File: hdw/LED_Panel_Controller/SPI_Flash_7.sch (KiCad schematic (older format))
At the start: 14 parts

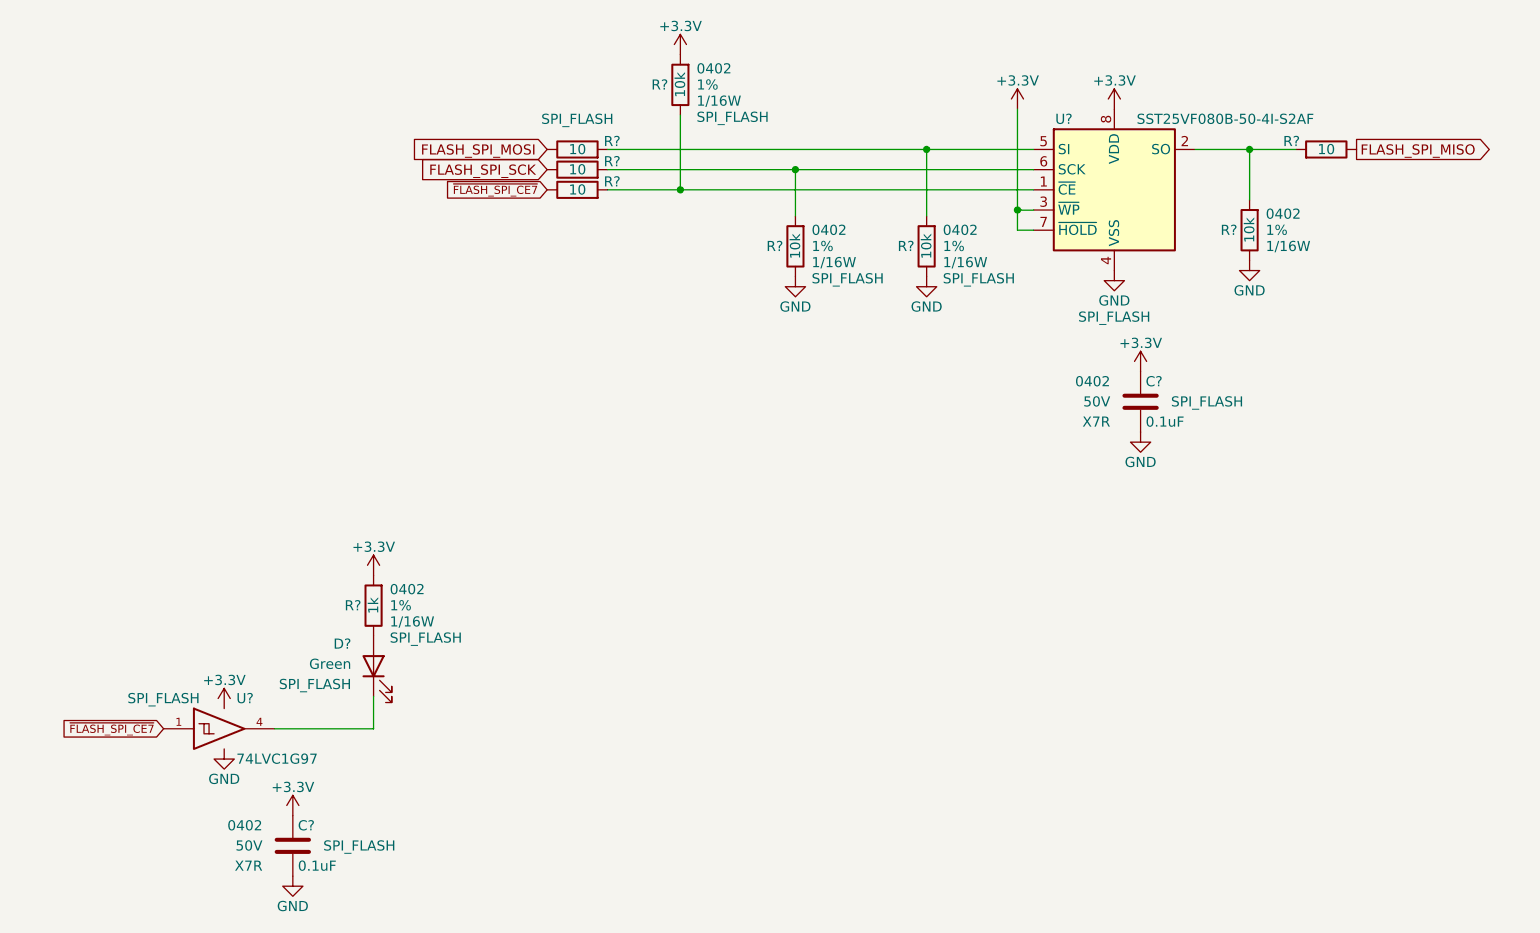
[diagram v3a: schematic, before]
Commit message: assigned I2C addresses
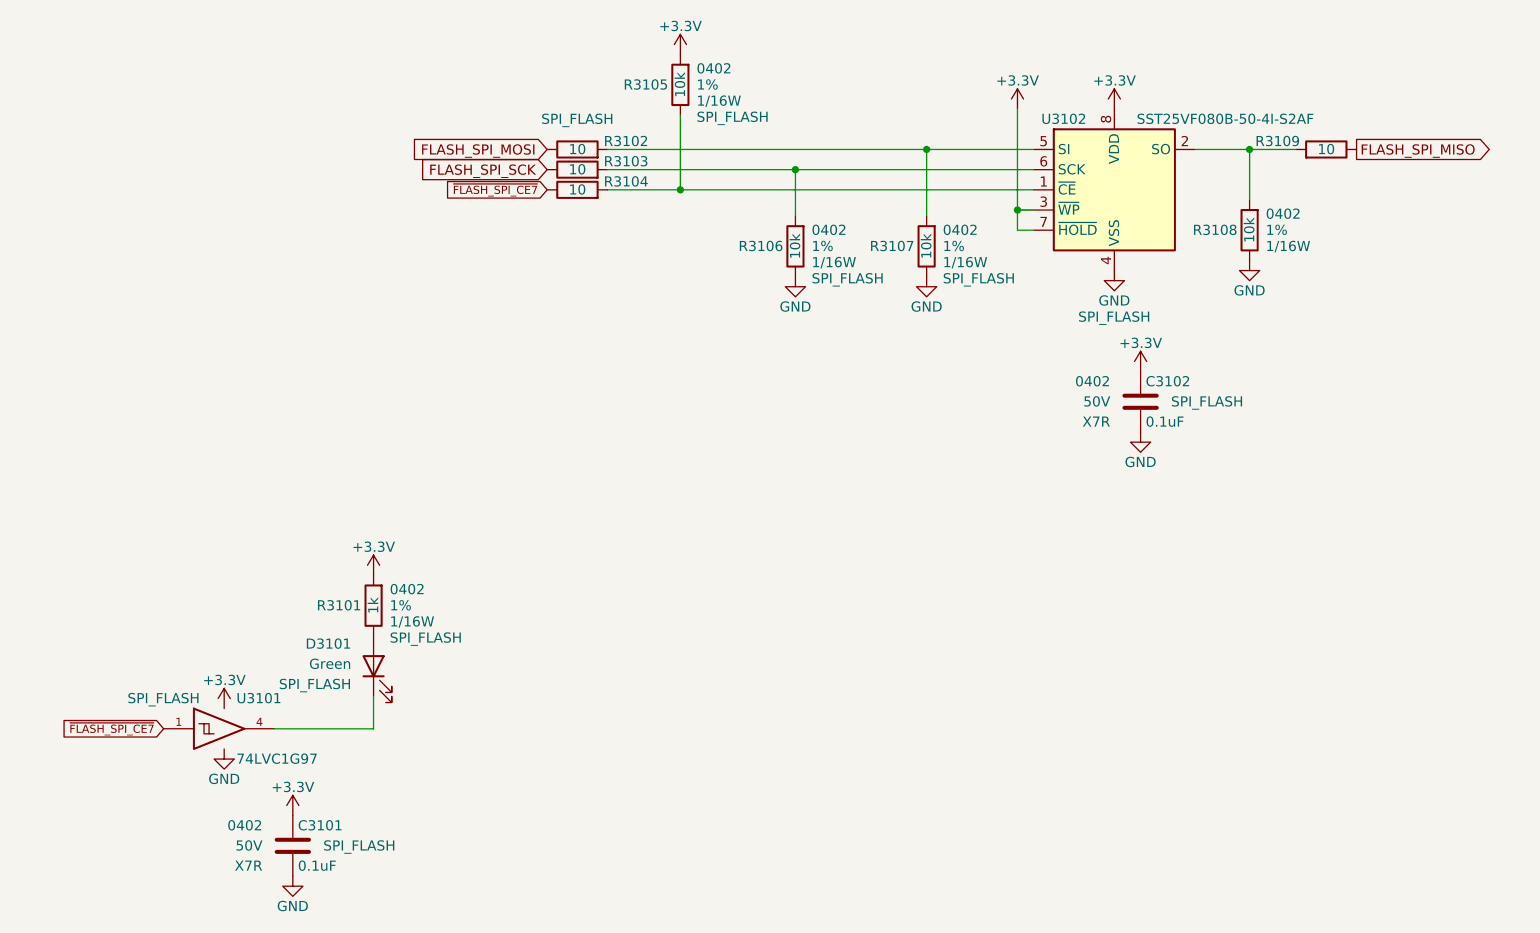
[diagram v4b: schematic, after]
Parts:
- removed C? (x2): 0.1uF, Capacitors_SMD:C_0402, symbol Custom_Library:C_Custom
- removed R? (x4): 10k, Resistors_SMD:R_0402, symbol Custom_Library:R_Custom
- removed R? (x4): 10, Resistors_SMD:R_0402, symbol Custom_Library:R_Custom
- removed R?: 1k, Resistors_SMD:R_0402, symbol Custom_Library:R_Custom
- removed U?: SST25VF080B-50-4I-S2AF, Package_SO:SOIC-8_5.275x5.275mm_P1.27mm, symbol Memory_Flash:SST25VF080B-50-4x-S2Ax
- removed U?: 74LVC1G97, Package_TO_SOT_SMD:SOT-363_SC-70-6, symbol Custom_Library:74LVC1G97_Power_BUF
- added C3101, C3102: 0.1uF, Capacitors_SMD:C_0402, symbol Custom_Library:C_Custom
- added R3101: 1k, Resistors_SMD:R_0402, symbol Custom_Library:R_Custom
- added R3102, R3103, R3104, R3109: 10, Resistors_SMD:R_0402, symbol Custom_Library:R_Custom
- added R3105, R3106, R3107, R3108: 10k, Resistors_SMD:R_0402, symbol Custom_Library:R_Custom
- added U3101: 74LVC1G97, Package_TO_SOT_SMD:SOT-363_SC-70-6, symbol Custom_Library:74LVC1G97_Power_BUF
- added U3102: SST25VF080B-50-4I-S2AF, Package_SO:SOIC-8_5.275x5.275mm_P1.27mm, symbol Memory_Flash:SST25VF080B-50-4x-S2Ax
- gave numbers to parts that had none: 1
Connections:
- net +3V3: now also C3101.1, C3102.1, R3101.1, R3105.1, U3101.5 (VCC), U3102.3 (~WP~), U3102.7 (~HOLD~), U3102.8 (VDD)
- net FLASH_SPI_MISO: now also R3109.2
- net FLASH_SPI_MOSI: now also R3102.2
- net FLASH_SPI_SCK: now also R3103.2
- net GND: now also C3101.2, C3102.2, R3106.2, R3107.2, R3108.2, U3101.2 (GND), U3101.3 (GND), U3101.6 (GND), U3102.4 (VSS)
- net ~FLASH_SPI_CE7: now also R3104.2, U3101.1
- net at D3101.1 (K): now also U3101.4
- net at D3101.2 (A): now also R3101.2
- new net: R3108.1, R3109.1, U3102.2 (SO)
- new net: R3102.1, R3107.1, U3102.5 (SI)
- new net: R3104.1, R3105.2, U3102.1 (~CE)
- new net: R3103.1, R3106.1, U3102.6 (SCK)
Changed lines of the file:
@@
 $EndDescr
 $Comp
-L power:GND #PWR?
-U 1 1 5BB4E0E3
+L power:GND #PWR03111
+U 1 1 60786263
 P 6080 4050
-F 0 "#PWR?" H 6080 3800 50  0001 C CNN
+F 0 "#PWR03111" H 6080 3800 50  0001 C CNN
 F 1 "GND" H 6080 3900 50  0000 C CNN
 F 2 "" H 6080 4050 50  0001 C CNN
@@
 $EndComp
 $Comp
-L Custom_Library:R_Custom R?
-U 1 1 5BB4EDD1
+L Custom_Library:R_Custom R3108
+U 1 1 60786265
 P 6750 3850
-F 0 "R?" H 6690 3850 50  0000 R CNN
+F 0 "R3108" H 6690 3850 50  0000 R CNN
 F 1 "10k" V 6750 3850 50  0000 C CNN
 F 2 "Resistors_SMD:R_0402" H 6750 3850 50  0001 C CNN
@@
 $EndComp
 $Comp
-L power:GND #PWR?
-U 1 1 5BB4EE63
+L power:GND #PWR03108
+U 1 1 6078626D
 P 5150 4080
-F 0 "#PWR?" H 5150 3830 50  0001 C CNN
+F 0 "#PWR03108" H 5150 3830 50  0001 C CNN
 F 1 "GND" H 5150 3930 50  0000 C CNN
 F 2 "" H 5150 4080 50  0001 C CNN
@@
 $EndComp
 $Comp
-L power:GND #PWR?
-U 1 1 5BB4EE7C
+L power:GND #PWR03114
+U 1 1 60786277
 P 6750 4000
-F 0 "#PWR?" H 6750 3750 50  0001 C CNN
+F 0 "#PWR03114" H 6750 3750 50  0001 C CNN
 F 1 "GND" H 6750 3850 50  0000 C CNN
 F 2 "" H 6750 4000 50  0001 C CNN
@@
 $EndComp
 $Comp
-L Custom_Library:R_Custom R?
-U 1 1 5BB4F53B
+L Custom_Library:R_Custom R3102
+U 1 1 6078627B
 P 3420 3450
-F 0 "R?" V 3380 3580 50  0000 L CNN
+F 0 "R3102" V 3380 3580 50  0000 L CNN
 F 1 "10" V 3420 3450 50  0000 C CNN
 F 2 "Resistors_SMD:R_0402" H 3420 3450 50  0001 C CNN
@@
 	3570 3650 3930 3650
 $Comp
-L power:+3.3V #PWR?
-U 1 1 5BDF3D33
+L power:+3.3V #PWR03106
+U 1 1 60786282
 P 3930 2980
-F 0 "#PWR?" H 3930 2830 50  0001 C CNN
+F 0 "#PWR03106" H 3930 2830 50  0001 C CNN
 F 1 "+3.3V" H 3930 3120 50  0000 C CNN
 F 2 "" H 3930 2980 50  0001 C CNN
@@
 $EndComp
 $Comp
-L power:+3.3V #PWR?
+L power:+3.3V #PWR03110
 U 1 1 5BDF3DF4
 P 6080 3250
-F 0 "#PWR?" H 6080 3100 50  0001 C CNN
+F 0 "#PWR03110" H 6080 3100 50  0001 C CNN
 F 1 "+3.3V" H 6080 3390 50  0000 C CNN
 F 2 "" H 6080 3250 50  0001 C CNN
@@
 $Comp
 L Custom_Library:C_Custom C?
-U 1 1 5C15F697
+U 1 1 6078628F
 P 2010 6900
-AR Path="/5BAAE16C/5C15F697" Ref="C?"  Part="1"
-AR Path="/5BB181D8/5C15F697" Ref="C?"  Part="1"
-AR Path="/5BB2595E/5C15F697" Ref="C?"  Part="1"
-AR Path="/5F583577/5C15F697" Ref="C?"  Part="1"
-AR Path="/5F5835B0/5C15F697" Ref="C?"  Part="1"
-F 0 "C?" H 2035 7000 50  0000 L CNN
+AR Path="/5BAAE16C/6078628F" Ref="C?"  Part="1"
+AR Path="/5BB181D8/6078628F" Ref="C?"  Part="1"
+AR Path="/5BB2595E/6078628F" Ref="C?"  Part="1"
+AR Path="/5F583577/6078628F" Ref="C?"  Part="1"
+AR Path="/5F5835B0/6078628F" Ref="C3101"  Part="1"
+F 0 "C3101" H 2035 7000 50  0000 L CNN
 F 1 "0.1uF" H 2035 6800 50  0000 L CNN
 F 2 "Capacitors_SMD:C_0402" H 2048 6750 50  0001 C CNN
@@
 $EndComp
 $Comp
-L power:+3.3V #PWR?
-U 1 1 5C161B83
+L power:+3.3V #PWR03101
+U 1 1 60786295
 P 1670 6220
-F 0 "#PWR?" H 1670 6070 50  0001 C CNN
+F 0 "#PWR03101" H 1670 6070 50  0001 C CNN
 F 1 "+3.3V" H 1670 6360 50  0000 C CNN
 F 2 "" H 1670 6220 50  0001 C CNN
@@
 $EndComp
 $Comp
-L power:+3.3V #PWR?
-U 1 1 5C161BE9
+L power:+3.3V #PWR03103
+U 1 1 6078629C
 P 2010 6750
-F 0 "#PWR?" H 2010 6600 50  0001 C CNN
+F 0 "#PWR03103" H 2010 6600 50  0001 C CNN
 F 1 "+3.3V" H 2010 6890 50  0000 C CNN
 F 2 "" H 2010 6750 50  0001 C CNN
@@
 $EndComp
 $Comp
-L power:GND #PWR?
-U 1 1 5C161C44
+L power:GND #PWR03104
+U 1 1 607862A8
 P 2010 7050
-F 0 "#PWR?" H 2010 6800 50  0001 C CNN
+F 0 "#PWR03104" H 2010 6800 50  0001 C CNN
 F 1 "GND" H 2010 6900 50  0000 C CNN
 F 2 "" H 2010 7050 50  0001 C CNN
@@
 $EndComp
 $Comp
-L power:GND #PWR?
-U 1 1 5C161C9F
+L power:GND #PWR03102
+U 1 1 607862B0
 P 1670 6420
-F 0 "#PWR?" H 1670 6170 50  0001 C CNN
+F 0 "#PWR03102" H 1670 6170 50  0001 C CNN
 F 1 "GND" H 1670 6270 50  0000 C CNN
 F 2 "" H 1670 6420 50  0001 C CNN
@@
 $Comp
 L power:+3.3V #PWR?
-U 1 1 5C166A81
+U 1 1 607862B6
 P 2410 5560
-AR Path="/5BB844FD/5C166A81" Ref="#PWR?"  Part="1"
-AR Path="/5BF346B3/5C166A81" Ref="#PWR?"  Part="1"
-AR Path="/5BB2595E/5C166A81" Ref="#PWR?"  Part="1"
-AR Path="/5F583577/5C166A81" Ref="#PWR?"  Part="1"
-AR Path="/5F5835B0/5C166A81" Ref="#PWR?"  Part="1"
-F 0 "#PWR?" H 2410 5410 50  0001 C CNN
+AR Path="/5BB844FD/607862B6" Ref="#PWR?"  Part="1"
+AR Path="/5BF346B3/607862B6" Ref="#PWR?"  Part="1"
+AR Path="/5BB2595E/607862B6" Ref="#PWR?"  Part="1"
+AR Path="/5F583577/607862B6" Ref="#PWR?"  Part="1"
+AR Path="/5F5835B0/607862B6" Ref="#PWR03105"  Part="1"
+F 0 "#PWR03105" H 2410 5410 50  0001 C CNN
 F 1 "+3.3V" H 2410 5700 50  0000 C CNN
 F 2 "" H 2410 5560 50  0001 C CNN
@@
 AR Path="/5BB2595E/5C166A95" Ref="D?"  Part="1"
 AR Path="/5F583577/5C166A95" Ref="D?"  Part="1"
-AR Path="/5F5835B0/5C166A95" Ref="D?"  Part="1"
-F 0 "D?" V 2520 6120 50  0000 L CNN
+AR Path="/5F5835B0/5C166A95" Ref="D3101"  Part="1"
+F 0 "D3101" V 2520 6120 50  0000 L CNN
 F 1 "Green" V 2420 6120 50  0000 L CNN
 F 2 "LEDs:LED_0402" H 2410 6010 50  0001 C CNN
@@
 $EndComp
 $Comp
-L Memory_Flash:SST25VF080B-50-4x-S2Ax U?
-U 1 1 5F6879D5
+L Memory_Flash:SST25VF080B-50-4x-S2Ax U3102
+U 1 1 607862FB
 P 6080 3650
-F 0 "U?" H 5830 4000 50  0000 C CNN
+F 0 "U3102" H 5830 4000 50  0000 C CNN
 F 1 "SST25VF080B-50-4I-S2AF" H 6630 4000 50  0000 C CNN
 F 2 "Package_SO:SOIC-8_5.275x5.275mm_P1.27mm" H 6080 2950 50  0001 C CNN
@@
 $EndComp
 $Comp
-L power:+3.3V #PWR?
-U 1 1 5F689292
+L power:+3.3V #PWR03112
+U 1 1 607862FD
 P 6210 4550
-F 0 "#PWR?" H 6210 4400 50  0001 C CNN
+F 0 "#PWR03112" H 6210 4400 50  0001 C CNN
 F 1 "+3.3V" H 6210 4690 50  0000 C CNN
 F 2 "" H 6210 4550 50  0001 C CNN
@@
 $EndComp
 $Comp
-L power:GND #PWR?
-U 1 1 5F689298
+L power:GND #PWR03113
+U 1 1 6078630A
 P 6210 4850
-F 0 "#PWR?" H 6210 4600 50  0001 C CNN
+F 0 "#PWR03113" H 6210 4600 50  0001 C CNN
 F 1 "GND" H 6210 4700 50  0000 C CNN
 F 2 "" H 6210 4850 50  0001 C CNN
@@
 $EndComp
 $Comp
-L power:+3.3V #PWR?
-U 1 1 5F69329F
+L power:+3.3V #PWR03109
+U 1 1 6078630E
 P 5600 3250
-F 0 "#PWR?" H 5600 3100 50  0001 C CNN
+F 0 "#PWR03109" H 5600 3100 50  0001 C CNN
 F 1 "+3.3V" H 5600 3390 50  0000 C CNN
 F 2 "" H 5600 3250 50  0001 C CNN
@@
 	3570 3550 4500 3550
 $Comp
-L Custom_Library:R_Custom R?
-U 1 1 5F697048
+L Custom_Library:R_Custom R3106
+U 1 1 60786315
 P 4500 3930
-F 0 "R?" H 4440 3930 50  0000 R CNN
+F 0 "R3106" H 4440 3930 50  0000 R CNN
 F 1 "10k" V 4500 3930 50  0000 C CNN
 F 2 "Resistors_SMD:R_0402" H 4500 3930 50  0001 C CNN
@@
 $EndComp
 $Comp
-L power:GND #PWR?
-U 1 1 5F697052
+L power:GND #PWR03107
+U 1 1 6078631A
 P 4500 4080
-F 0 "#PWR?" H 4500 3830 50  0001 C CNN
+F 0 "#PWR03107" H 4500 3830 50  0001 C CNN
 F 1 "GND" H 4500 3930 50  0000 C CNN
 F 2 "" H 4500 4080 50  0001 C CNN
@@
 	4500 3550 5680 3550
 $Comp
-L Custom_Library:R_Custom R?
-U 1 1 5F7379BB
+L Custom_Library:R_Custom R3103
+U 1 1 60786323
 P 3420 3550
-F 0 "R?" V 3380 3680 50  0000 L CNN
+F 0 "R3103" V 3380 3680 50  0000 L CNN
 F 1 "10" V 3420 3550 50  0000 C CNN
 F 2 "Resistors_SMD:R_0402" H 3420 3550 50  0001 C CNN
@@
 $EndComp
 $Comp
-L Custom_Library:R_Custom R?
-U 1 1 5F737B74
+L Custom_Library:R_Custom R3104
+U 1 1 60786327
 P 3420 3650
-F 0 "R?" V 3380 3780 50  0000 L CNN
+F 0 "R3104" V 3380 3780 50  0000 L CNN
 F 1 "10" V 3420 3650 50  0000 C CNN
 F 2 "Resistors_SMD:R_0402" H 3420 3650 50  0001 C CNN
@@
 $EndComp
 $Comp
-L Custom_Library:R_Custom R?
-U 1 1 5F737D15
+L Custom_Library:R_Custom R3109
+U 1 1 60786334
 P 7130 3450
-F 0 "R?" V 7090 3580 50  0000 L CNN
+F 0 "R3109" V 7090 3580 50  0000 L CNN
 F 1 "10" V 7130 3450 50  0000 C CNN
 F 2 "Resistors_SMD:R_0402" H 7130 3450 50  0001 C CNN
@@
 $EndComp
 $Comp
-L Custom_Library:74LVC1G97_Power_BUF U?
-U 1 1 5FE9D8D5
+L Custom_Library:74LVC1G97_Power_BUF U3101
+U 1 1 60786343
 P 1670 6320
-F 0 "U?" H 1730 6470 50  0000 L CNN
+F 0 "U3101" H 1730 6470 50  0000 L CNN
 F 1 "74LVC1G97" H 1730 6170 50  0000 L CNN
 F 2 "Package_TO_SOT_SMD:SOT-363_SC-70-6" H 1720 6320 50  0001 C CNN
@@
 $EndComp
 $Comp
-L Custom_Library:R_Custom R?
-U 1 1 6026393A
+L Custom_Library:R_Custom R3107
+U 1 1 60786357
 P 5150 3930
-F 0 "R?" H 5090 3930 50  0000 R CNN
+F 0 "R3107" H 5090 3930 50  0000 R CNN
 F 1 "10k" V 5150 3930 50  0000 C CNN
 F 2 "Resistors_SMD:R_0402" H 5150 3930 50  0001 C CNN
@@
 $EndComp
 $Comp
-L Custom_Library:R_Custom R?
-U 1 1 60263FB7
+L Custom_Library:R_Custom R3105
+U 1 1 6078635E
 P 3930 3130
-F 0 "R?" H 3870 3130 50  0000 R CNN
+F 0 "R3105" H 3870 3130 50  0000 R CNN
 F 1 "10k" V 3930 3130 50  0000 C CNN
 F 2 "Resistors_SMD:R_0402" H 3930 3130 50  0001 C CNN
@@
 $EndComp
 $Comp
-L Custom_Library:R_Custom R?
-U 1 1 60266213
+L Custom_Library:R_Custom R3101
+U 1 1 60786365
 P 2410 5710
-F 0 "R?" H 2350 5710 50  0000 R CNN
+F 0 "R3101" H 2350 5710 50  0000 R CNN
 F 1 "1k" V 2410 5710 50  0000 C CNN
 F 2 "Resistors_SMD:R_0402" H 2410 5710 50  0001 C CNN
@@
 $Comp
 L Custom_Library:C_Custom C?
-U 1 1 60269564
+U 1 1 60786370
 P 6210 4700
-AR Path="/5BAAE16C/60269564" Ref="C?"  Part="1"
-AR Path="/5BB181D8/60269564" Ref="C?"  Part="1"
-AR Path="/5BB2595E/60269564" Ref="C?"  Part="1"
-AR Path="/5F583577/60269564" Ref="C?"  Part="1"
-AR Path="/5F5835B0/60269564" Ref="C?"  Part="1"
-F 0 "C?" H 6235 4800 50  0000 L CNN
+AR Path="/5BAAE16C/60786370" Ref="C?"  Part="1"
+AR Path="/5BB181D8/60786370" Ref="C?"  Part="1"
+AR Path="/5BB2595E/60786370" Ref="C?"  Part="1"
+AR Path="/5F583577/60786370" Ref="C?"  Part="1"
+AR Path="/5F5835B0/60786370" Ref="C3102"  Part="1"
+F 0 "C3102" H 6235 4800 50  0000 L CNN
 F 1 "0.1uF" H 6235 4600 50  0000 L CNN
 F 2 "Capacitors_SMD:C_0402" H 6248 4550 50  0001 C CNN
